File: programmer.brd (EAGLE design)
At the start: 45.7 x 20.3 mm, 20 parts, among them U1 ATMEGA8U2AU, X1 16MHz

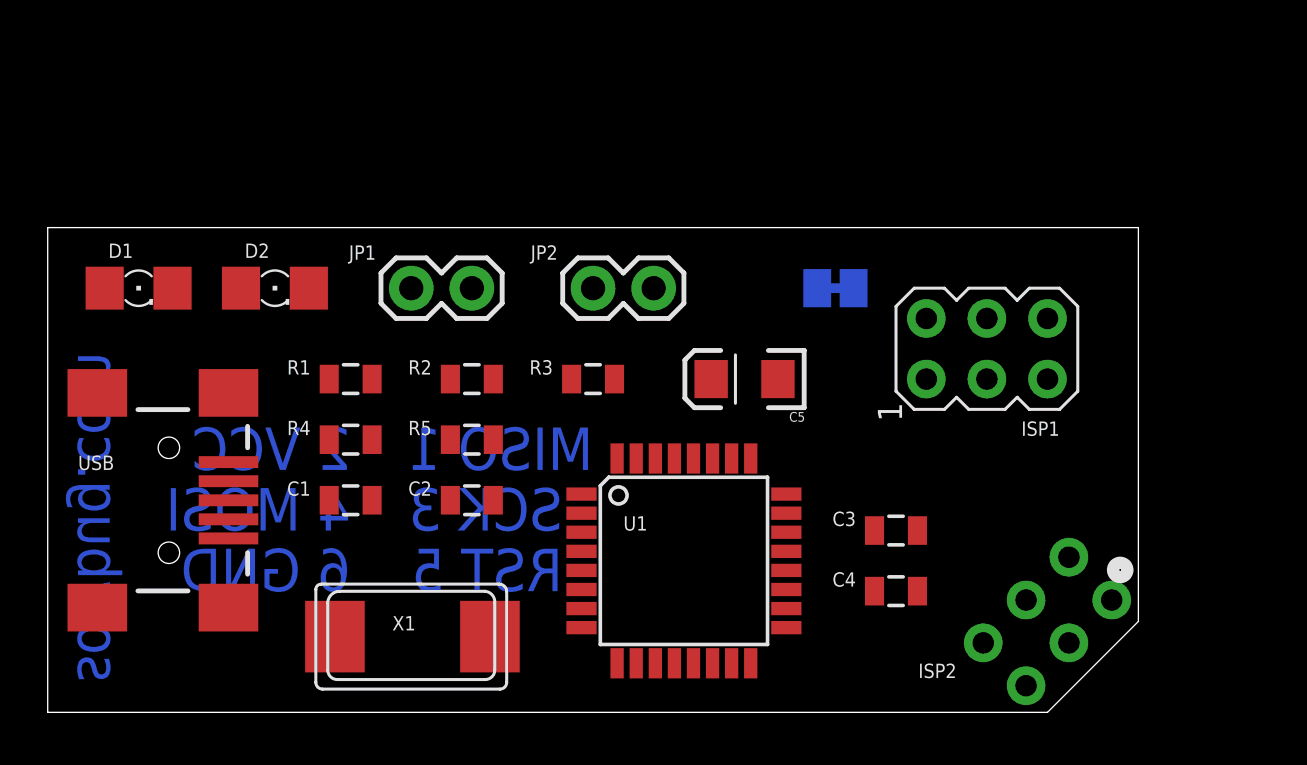
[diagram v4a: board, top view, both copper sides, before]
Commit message: Better routing setup. Moved SJ1 jumper temporarily.
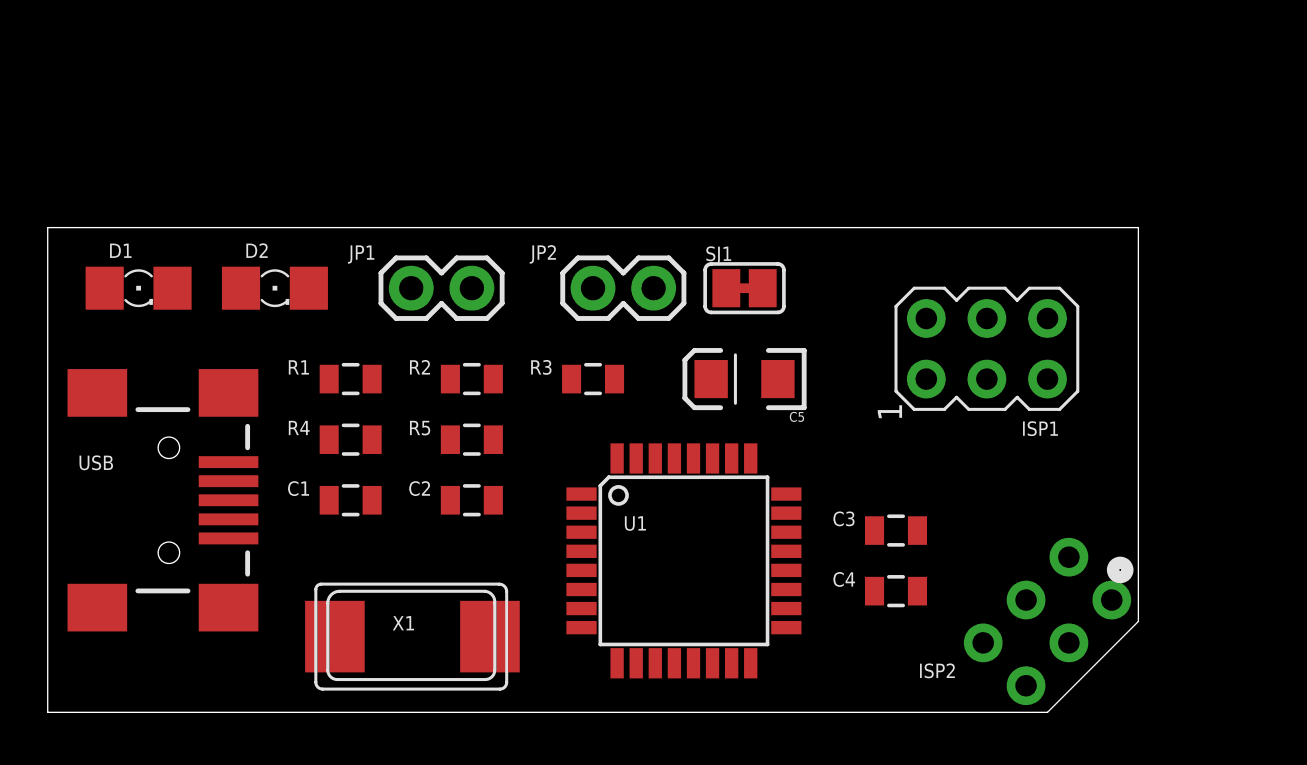
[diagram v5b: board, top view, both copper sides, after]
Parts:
- moved SJ1 3.81 mm to (29.2, 17.8), flipped to the top
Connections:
- net 5V: now also SJ1.1; no longer SJ1.2
- net VCC: now also SJ1.2; no longer SJ1.1
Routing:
- net N$4: track 1.27 -> 0.00 mm
- net SJ1-CONN: track 0.00 -> 1.27 mm
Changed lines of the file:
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@@
 <wire x1="45.72" y1="20.32" x2="0" y2="20.32" width="0" layer="20"/>
 <wire x1="0" y1="20.32" x2="0" y2="0" width="0" layer="20"/>
-<text x="1.27" y="1.27" size="1.778" layer="16" font="vector" rot="MR90">sowbug.com</text>
-<text x="22.86" y="10.16" size="1.778" layer="16" font="vector" rot="MR0">MISO 1</text>
-<text x="12.7" y="10.16" size="1.778" layer="16" font="vector" rot="MR0">2 VCC</text>
-<text x="21.59" y="7.62" size="1.778" layer="16" font="vector" rot="MR0">SCK 3</text>
-<text x="12.7" y="7.62" size="1.778" layer="16" font="vector" rot="MR0">4 MOSI</text>
-<text x="21.59" y="5.08" size="1.778" layer="16" font="vector" rot="MR0">RST 5</text>
-<text x="12.7" y="5.08" size="1.778" layer="16" font="vector" rot="MR0">6 GND</text>
+<text x="1.27" y="1.27" size="1.778" layer="22" font="vector" rot="MR90">sowbug.com</text>
+<text x="22.86" y="10.16" size="1.778" layer="22" font="vector" rot="MR0">MISO 1</text>
+<text x="12.7" y="10.16" size="1.778" layer="22" font="vector" rot="MR0">2 VCC</text>
+<text x="21.59" y="7.62" size="1.778" layer="22" font="vector" rot="MR0">SCK 3</text>
+<text x="12.7" y="7.62" size="1.778" layer="22" font="vector" rot="MR0">4 MOSI</text>
+<text x="21.59" y="5.08" size="1.778" layer="22" font="vector" rot="MR0">RST 5</text>
+<text x="12.7" y="5.08" size="1.778" layer="22" font="vector" rot="MR0">6 GND</text>
 <circle x="44.958" y="5.969" radius="0.254" width="0.6096" layer="25"/>
 </plain>
@@
 <autorouter>
 <pass name="Default">
-<param name="RoutingGrid" value="10mil"/>
-<param name="tpViaShape" value="round"/>
+<param name="RoutingGrid" value="12.5mil"/>
+<param name="tpViaShape" value="octagon"/>
 <param name="PrefDir.1" value="|"/>
 <param name="PrefDir.2" value="0"/>
@@
 <attribute name="VALUE" x="18.034" y="12.573" size="0.6" layer="27"/>
 </element>
-<element name="SJ1" library="jumper" package="SJ" value="VCC-5V" x="33.02" y="17.78" smashed="yes" rot="MR0">
-<attribute name="NAME" x="34.671" y="18.923" size="0.6" layer="26" ratio="10" rot="MR0"/>
-<attribute name="VALUE" x="32.6199" y="17.78" size="0.02" layer="28" rot="MR0"/>
+<element name="SJ1" library="jumper" package="SJ" value="VCC-5V" x="29.21" y="17.78" smashed="yes">
+<attribute name="NAME" x="27.559" y="18.923" size="0.6" layer="25" ratio="10"/>
+<attribute name="VALUE" x="29.6101" y="17.78" size="0.02" layer="27"/>
 </element>
 <element name="C5" library="SparkFun" package="EIA3216" value="10 uF" x="29.21" y="13.97" rot="R180"/>
@@
 <contactref element="U1" pad="4"/>
 <contactref element="U1" pad="32"/>
-<contactref element="SJ1" pad="1"/>
+<contactref element="SJ1" pad="2"/>
 <contactref element="C5" pad="A"/>
 <contactref element="C3" pad="2"/>
-<wire x1="33.782" y1="17.78" x2="36.83" y2="16.51" width="0" layer="19" extent="16-16"/>
-<wire x1="27.81" y1="13.97" x2="33.782" y2="17.78" width="0" layer="19" extent="1-16"/>
+<wire x1="29.972" y1="17.78" x2="36.83" y2="16.51" width="0" layer="19" extent="1-1"/>
+<wire x1="27.81" y1="13.97" x2="29.972" y2="17.78" width="0" layer="19" extent="1-1"/>
 <wire x1="25.4" y1="17.78" x2="27.81" y2="13.97" width="0" layer="19" extent="1-1"/>
 <wire x1="21.96" y1="13.97" x2="25.4" y2="17.78" width="0" layer="19" extent="1-1"/>
@@
 <contactref element="USB" pad="VBUS"/>
 <contactref element="JP2" pad="1"/>
-<contactref element="SJ1" pad="2"/>
-<wire x1="22.86" y1="17.78" x2="32.258" y2="17.78" width="0" layer="19" extent="16-16"/>
+<contactref element="SJ1" pad="1"/>
+<wire x1="22.86" y1="17.78" x2="28.448" y2="17.78" width="0" layer="19" extent="1-1"/>
 <wire x1="24.67" y1="10.6426" x2="22.86" y2="17.78" width="0" layer="19" extent="1-1"/>
 <wire x1="7.58" y1="10.49" x2="22.86" y2="17.78" width="0" layer="19" extent="1-1"/>
@@
 <wire x1="22.3774" y1="4.35" x2="10.947" y2="17.78" width="0" layer="19" extent="1-1"/>
 </signal>
-<signal name="N$4">
-<wire x1="33.655" y1="17.78" x2="32.385" y2="17.78" width="0.4064" layer="16"/>
+<signal name="SJ1-CONN">
+<wire x1="28.575" y1="17.78" x2="29.845" y2="17.78" width="0.4064" layer="1"/>
 </signal>
 </signals>

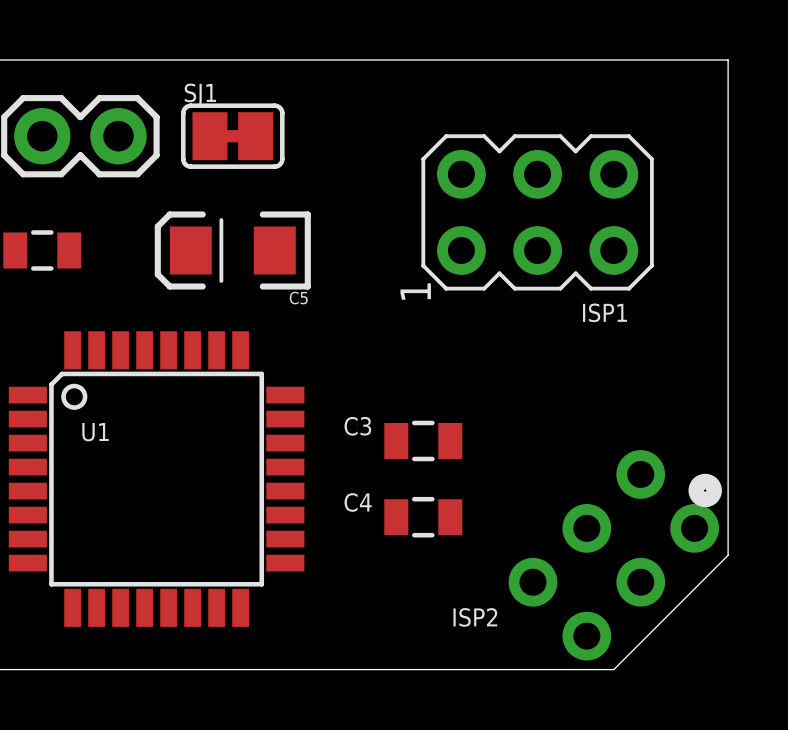
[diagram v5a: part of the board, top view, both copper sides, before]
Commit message: Nudge here and there to get rid of DRC errors.
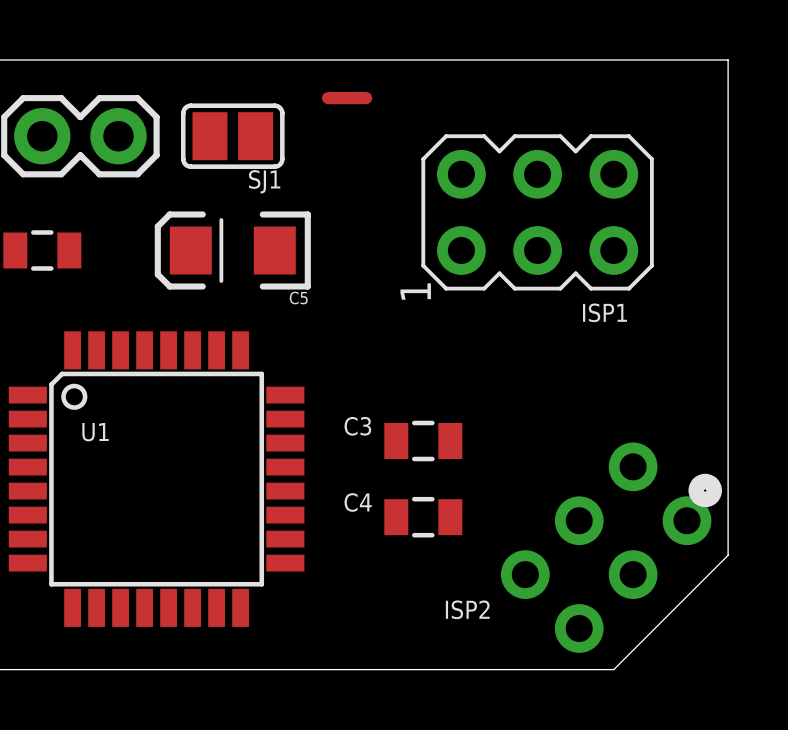
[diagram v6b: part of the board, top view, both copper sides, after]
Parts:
- moved ISP2 0.36 mm to (41.7, 4.06)
- turned SJ1 to 180 degrees
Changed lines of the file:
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@@
 <attribute name="NAME" x="42.418" y="12.192" size="0.6" layer="25" rot="R180"/>
 </element>
-<element name="ISP2" library="adafruit" package="AVRISP" value="AVRISP-6" x="41.91" y="3.81" smashed="yes" rot="MR45">
-<attribute name="NAME" x="38.1" y="2.039475" size="0.6" layer="25" rot="R180"/>
+<element name="ISP2" library="adafruit" package="AVRISP" value="AVRISP-6" x="41.656" y="4.064" smashed="yes" rot="MR45">
+<attribute name="NAME" x="37.846" y="2.293475" size="0.6" layer="25" rot="R180"/>
 </element>
 <element name="R4" library="SparkFun" package="0805" value="22" x="12.7" y="11.43" smashed="yes">
@@
 <attribute name="VALUE" x="18.034" y="12.573" size="0.6" layer="27"/>
 </element>
-<element name="SJ1" library="jumper" package="SJ" value="VCC-5V" x="29.21" y="17.78" smashed="yes">
-<attribute name="NAME" x="27.559" y="18.923" size="0.6" layer="25" ratio="10"/>
-<attribute name="VALUE" x="29.6101" y="17.78" size="0.02" layer="27"/>
+<element name="SJ1" library="jumper" package="SJ" value="VCC-5V" x="29.21" y="17.78" smashed="yes" rot="R180">
+<attribute name="NAME" x="30.861" y="16.637" size="0.6" layer="25" ratio="10" rot="R180"/>
+<attribute name="VALUE" x="28.8099" y="17.78" size="0.02" layer="27" rot="R180"/>
 </element>
 <element name="C5" library="SparkFun" package="EIA3216" value="10 uF" x="29.21" y="13.97" rot="R180"/>
@@
 <contactref element="C5" pad="A"/>
 <contactref element="C3" pad="2"/>
-<wire x1="29.972" y1="17.78" x2="36.83" y2="16.51" width="0" layer="19" extent="1-1"/>
-<wire x1="27.81" y1="13.97" x2="29.972" y2="17.78" width="0" layer="19" extent="1-1"/>
-<wire x1="25.4" y1="17.78" x2="27.81" y2="13.97" width="0" layer="19" extent="1-1"/>
+<wire x1="28.448" y1="17.78" x2="36.83" y2="16.51" width="0" layer="19" extent="1-1"/>
+<wire x1="25.4" y1="17.78" x2="28.448" y2="17.78" width="0" layer="19" extent="1-1"/>
+<wire x1="27.81" y1="13.97" x2="28.448" y2="17.78" width="0" layer="19" extent="1-1"/>
 <wire x1="21.96" y1="13.97" x2="25.4" y2="17.78" width="0" layer="19" extent="1-1"/>
 <wire x1="18.68" y1="13.97" x2="21.96" y2="13.97" width="0" layer="19" extent="1-1"/>
@@
 <wire x1="11.8" y1="13.97" x2="18.68" y2="13.97" width="0" layer="19" extent="1-1"/>
 <wire x1="36.46" y1="7.62" x2="36.83" y2="16.51" width="0" layer="19" extent="1-1"/>
-<wire x1="42.808028125" y1="6.504075" x2="36.46" y2="7.62" width="0" layer="19" extent="1-1"/>
+<wire x1="42.554028125" y1="6.758075" x2="36.46" y2="7.62" width="0" layer="19" extent="1-1"/>
 </signal>
 <signal name="GND">
@@
 <wire x1="34.66" y1="7.62" x2="41.91" y2="16.51" width="0" layer="19" extent="1-1"/>
 <wire x1="34.66" y1="5.08" x2="34.66" y2="7.62" width="0" layer="19" extent="1-1"/>
-<wire x1="39.215925" y1="2.911971875" x2="34.66" y2="5.08" width="0" layer="19" extent="1-1"/>
+<wire x1="38.961925" y1="3.165971875" x2="34.66" y2="5.08" width="0" layer="19" extent="1-1"/>
 <wire x1="30.61" y1="13.97" x2="34.66" y2="7.62" width="0" layer="19" extent="1-1"/>
 <wire x1="27.07" y1="10.6426" x2="30.61" y2="13.97" width="0" layer="19" extent="1-1"/>
@@
 <contactref element="ISP1" pad="3"/>
 <contactref element="ISP2" pad="3"/>
-<wire x1="42.808028125" y1="2.911971875" x2="39.37" y2="13.97" width="0" layer="19" extent="1-1"/>
-<wire x1="28.67" y1="2.0574" x2="42.808028125" y2="2.911971875" width="0" layer="19" extent="1-1"/>
+<wire x1="42.554028125" y1="3.165971875" x2="39.37" y2="13.97" width="0" layer="19" extent="1-1"/>
+<wire x1="28.67" y1="2.0574" x2="42.554028125" y2="3.165971875" width="0" layer="19" extent="1-1"/>
 </signal>
 <signal name="3.3V">
@@
 <contactref element="JP2" pad="1"/>
 <contactref element="SJ1" pad="1"/>
-<wire x1="22.86" y1="17.78" x2="28.448" y2="17.78" width="0" layer="19" extent="1-1"/>
+<wire x1="22.86" y1="17.78" x2="29.972" y2="17.78" width="0" layer="19" extent="1-1"/>
 <wire x1="24.67" y1="10.6426" x2="22.86" y2="17.78" width="0" layer="19" extent="1-1"/>
 <wire x1="7.58" y1="10.49" x2="22.86" y2="17.78" width="0" layer="19" extent="1-1"/>
@@
 <wire x1="30.9626" y1="9.15" x2="41.91" y2="13.97" width="0" layer="19" extent="1-1"/>
 <wire x1="30.9626" y1="4.35" x2="30.9626" y2="9.15" width="0" layer="19" extent="1-1"/>
-<wire x1="41.011975" y1="1.115921875" x2="30.9626" y2="4.35" width="0" layer="19" extent="1-1"/>
+<wire x1="40.757975" y1="1.369921875" x2="30.9626" y2="4.35" width="0" layer="19" extent="1-1"/>
 <wire x1="17.78" y1="17.78" x2="30.9626" y2="9.15" width="0" layer="19" extent="1-1"/>
 </signal>
@@
 <contactref element="ISP1" pad="1"/>
 <contactref element="U1" pad="17"/>
+<wire x1="44.350078125" y1="4.962025" x2="36.83" y2="13.97" width="0" layer="19" extent="1-1"/>
 <wire x1="30.9626" y1="3.55" x2="36.83" y2="13.97" width="0" layer="19" extent="1-1"/>
-<wire x1="44.604078125" y1="4.708025" x2="36.83" y2="13.97" width="0" layer="19" extent="1-1"/>
 </signal>
 <signal name="MOSI">
@@
 <contactref element="ISP2" pad="4"/>
 <contactref element="U1" pad="16"/>
-<wire x1="41.011975" y1="4.708025" x2="39.37" y2="16.51" width="0" layer="19" extent="1-1"/>
-<wire x1="29.47" y1="2.0574" x2="41.011975" y2="4.708025" width="0" layer="19" extent="1-1"/>
+<wire x1="40.757975" y1="4.962025" x2="39.37" y2="16.51" width="0" layer="19" extent="1-1"/>
+<wire x1="29.47" y1="2.0574" x2="40.757975" y2="4.962025" width="0" layer="19" extent="1-1"/>
 </signal>
 <signal name="N$1">
@@
 </signal>
 <signal name="SJ1-CONN">
-<wire x1="28.575" y1="17.78" x2="29.845" y2="17.78" width="0.4064" layer="1"/>
+<wire x1="32.385" y1="19.05" x2="33.655" y2="19.05" width="0.4064" layer="1"/>
 </signal>
 </signals>

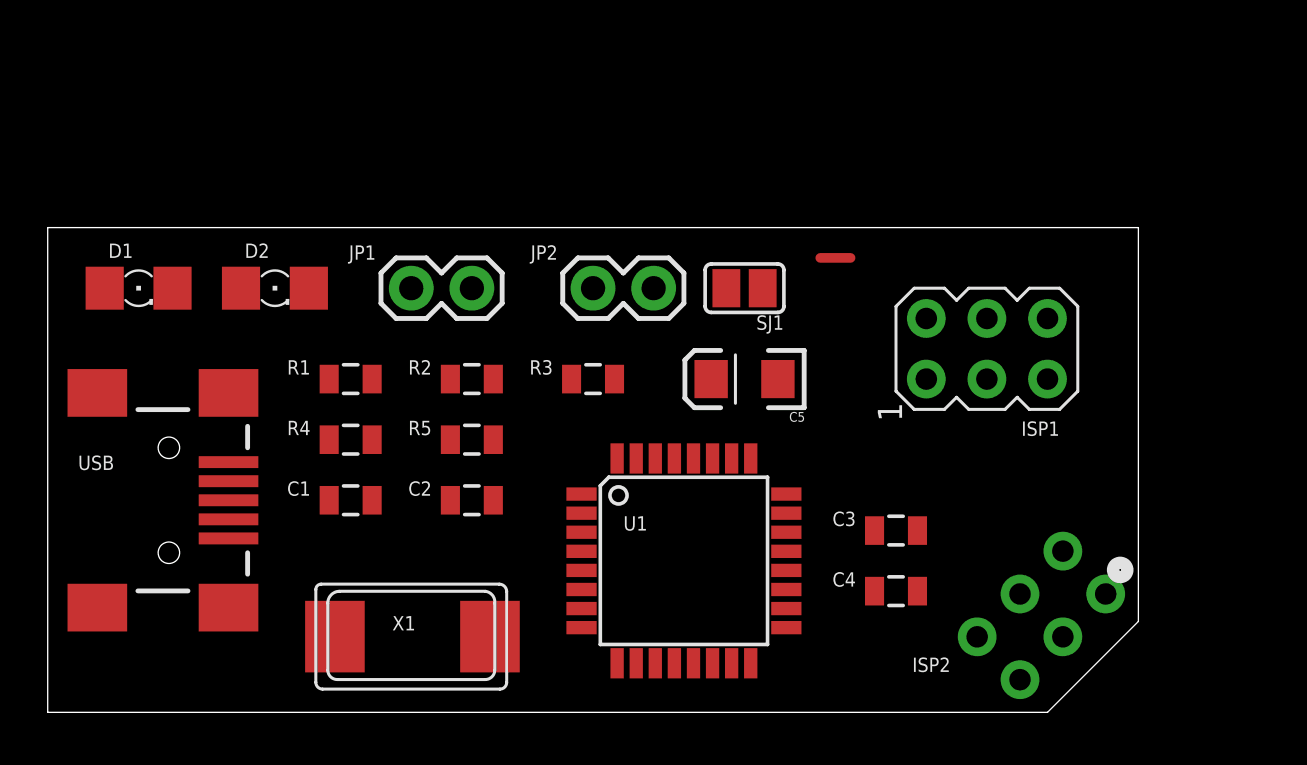
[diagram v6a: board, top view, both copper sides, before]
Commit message: Fixed error in self-program jumper. Balanced components.
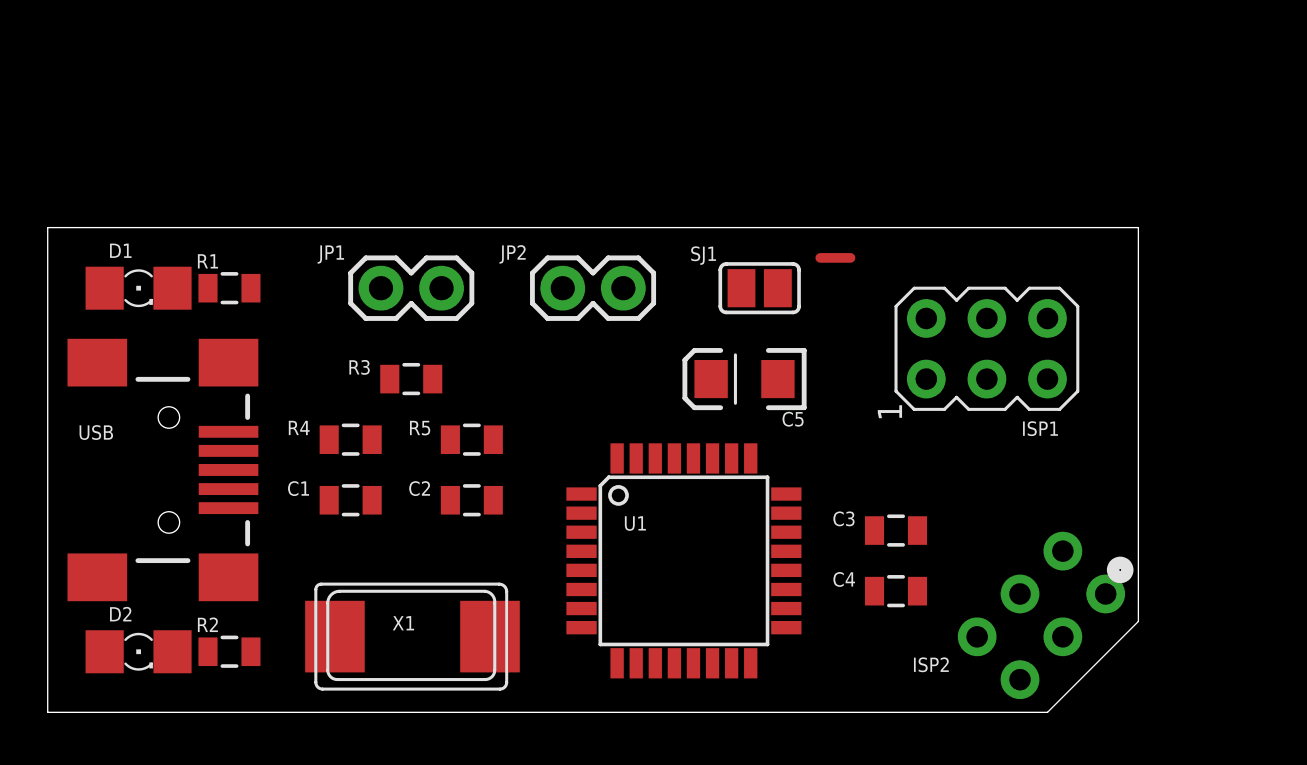
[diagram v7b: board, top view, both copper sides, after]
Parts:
- C4: value 0.1 uF -> 1 uF
- moved D2 16.3 mm to (3.81, 2.54)
- moved R2 15.3 mm to (7.62, 2.54)
- moved R3 7.62 mm to (15.2, 14.0)
- moved R1 6.35 mm to (7.62, 17.8)
- moved JP1 1.27 mm to (14.0, 17.8)
- moved JP2 1.27 mm to (21.6, 17.8)
- moved USB 1.27 mm to (5.08, 10.2)
- moved SJ1 0.63 mm to (29.8, 17.8), turned to 0 degrees
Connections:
- removed net RST_JP1: JP1.1, R3.2
- new net BUFF-OE: U1.10
- new net RST-PU: JP1.1, R3.2, U1.24
- net N$3: now also R1.1; no longer R1.2
- net RST: no longer U1.24
- net VCC: now also R1.2; no longer R1.1

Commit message: Removed BUFF-OE.
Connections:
- removed net BUFF-OE: U1.10
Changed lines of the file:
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@@
 <wire x1="13.97" y1="17.78" x2="16.14" y2="13.97" width="0" layer="19" extent="1-1"/>
-</signal>
-<signal name="BUFF-OE">
-<contactref element="U1" pad="10"/>
 </signal>
 </signals>
